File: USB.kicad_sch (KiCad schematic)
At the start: 29 parts, among them J11 USB3_A, J12 USB3_A, Q1 TCKE800NL, U14 USB5734_MR, Y3 25Mhz

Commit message: change cad data
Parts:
- removed R44: 10kΩ, Resistor_SMD:R_0603_1608Metric_Pad0.98x0.95mm_HandSolder, symbol Device:R
- removed U14: USB5734_MR, CM5IO:QFN50P900X900X100-65N, symbol USB5734:USB5734_MR
- added C137, C138, C139, C140, C142, C143, C144, C145, C87: 0.1uF, Capacitor_SMD:C_0402_1005Metric_Pad0.74x0.62mm_HandSolder, symbol Device:C
- added FB1: FerriteBead, Inductor_SMD:L_0603_1608Metric_Pad1.05x0.95mm_HandSolder, symbol Device:FerriteBead
- added R62: 320kΩ, Resistor_SMD:R_0603_1608Metric_Pad0.98x0.95mm_HandSolder, symbol Device:R
- added U15: USB5744_2G, CM5IO:VQFN56_2G_MCH, symbol USB5744:USB5744_2G
- C36: renamed from C22; footprint Capacitor_SMD:C_0603_1608Metric_Pad1.08x0.95mm_HandSolder -> Capacitor_SMD:C_0402_1005Metric_Pad0.74x0.62mm_HandSolder
- Y4: renamed from Y3; footprint Crystal:Crystal_SMD_SeikoEpson_FA238-4Pin_3.2x2.5mm -> Crystal:Crystal_SMD_SeikoEpson_FA128-4Pin_2.0x1.6mm
- renumbered C85 to C101, C87 to C105, C79 to C106, C96 to C118, C95 to C119, C97 to C120, C94 to C121, C23 to C37, C24 to C38, C25 to C39, C27 to C41, C28 to C42, C29 to C43, C51 to C73, C52 to C74, C62 to C82, C59 to C83, C60 to C84, C61 to C85, C75 to C99, R7 to R17, R42 to R53
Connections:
- net +3.3V: now also FB1.1; no longer C105.1, C120.1, C82.1, C84.1
- net 1.2V: now also U15.12 (VDD12__1), U15.15 (VDD12__2), U15.21 (VDD12__3), U15.28 (VDD12__4), U15.33 (VDD12__5), U15.43 (VDD12__6), U15.49 (VDD12__7), U15.5 (VDD12)
- net GND: now also C87.2, U15.52 (ATEST), U15.57 (VSS)
- net SS_RX_N: now also U15.51 (USB3UP_RXDM)
- net SS_RX_P: now also U15.50 (USB3UP_RXDP)
- net SS_TX_N: now also U15.48 (USB3UP_TXDM)
- net SS_TX_P: now also U15.47 (USB3UP_TXDP)
- net USB3-0-D_N: now also U15.2 (USB2DN_DM1/PRT_DIS_M1)
- net USB3-0-D_P: now also U15.1 (USB2DN_DP1/PRT_DIS_P1)
- net USB3-0-RX_N: now also U15.7 (USB3DN_RXDM1)
- net USB3-0-RX_P: now also U15.6 (USB3DN_RXDP1)
- net USB3-0-TX_N: now also C144.1, U15.4 (USB3DN_TXDM1); no longer J12.A8 (SSTX-)
- net USB3-0-TX_P: now also C145.1, U15.3 (USB3DN_TXDP1); no longer J12.A9 (SSTX+)
- net USB3-1-D_N: now also U15.9 (USB2DN_DM2/PRT_DIS_M2)
- net USB3-1-D_P: now also U15.8 (USB2DN_DP2/PRT_DIS_P2)
- net USB3-1-RX_N: now also U15.14 (USB3DN_RXDM2)
- net USB3-1-RX_P: now also U15.13 (USB3DN_RXDP2)
- net USB3-1-TX_N: now also C138.1, U15.11 (USB3DN_TXDM2); no longer J12.B9 (SSTX+)
- net USB3-1-TX_P: now also C137.1, U15.10 (USB3DN_TXDP2); no longer J12.B8 (SSTX-)
- net USB3-2-D_N: now also U15.18 (USB2DN_DM3/PRT_DIS_M3)
- net USB3-2-D_P: now also U15.17 (USB2DN_DP3/PRT_DIS_P3)
- net USB3-2-RX_N: now also U15.23 (USB3DN_RXDM3)
- net USB3-2-RX_P: now also U15.22 (USB3DN_RXDP3)
- net USB3-2-TX_N: now also C140.1, U15.20 (USB3DN_TXDM3); no longer J11.B9 (SSTX+)
- net USB3-2-TX_P: now also C139.1, U15.19 (USB3DN_TXDP3); no longer J11.B8 (SSTX-)
- net USB3-3-D_N: now also U15.25 (USB2DN_DM4/PRT_DIS_M4)
- net USB3-3-D_P: now also U15.24 (USB2DN_DP4/PRT_DIS_P4)
- net USB3-3-RX_N: now also U15.30 (USB3DN_RXDM4)
- net USB3-3-RX_P: now also U15.29 (USB3DN_RXDP4)
- net USB3-3-TX_N: now also C142.1, U15.27 (USB3DN_TXDM4); no longer J11.A8 (SSTX-)
- net USB3-3-TX_P: now also C143.1, U15.26 (USB3DN_TXDP4); no longer J11.A9 (SSTX+)
- net USB_DN: now also U15.46 (USB2UP_DM)
- net USB_DP: now also U15.45 (USB2UP_DP)
- net at C74.1, Y4.3: now also U15.53 (XTALO)
- net at C73.1, Y4.1: now also U15.54 (XTALI/CLK_IN)
- net at R53.2: now also U15.56 (RBIAS)
- new net: C87.1, R62.1, U15.42 (RESET_N)
- new net: C139.2, J11.B8 (SSTX-)
- new net: C140.2, J11.B9 (SSTX+)
- new net: C137.2, J12.B8 (SSTX-)
- new net: C143.2, J11.A9 (SSTX+)
- new net: C144.2, J12.A8 (SSTX-)
- new net: C142.2, J11.A8 (SSTX-)
- new net: C145.2, J12.A9 (SSTX+)
- new net: C138.2, J12.B9 (SSTX+)
- new net 3.3V: C105.1, C120.1, C82.1, C84.1, FB1.2, R62.2, U15.16 (VDD33), U15.31 (VDD33__1), U15.37 (VBUS_DET/GPIO16), U15.44 (VDD33__2), U15.55 (VDD33__3)
- no-connect marks 0 -> 4
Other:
- moved on the sheet: C105, C120, C73, C74, C82, C84, J11, J12, R53, Y4

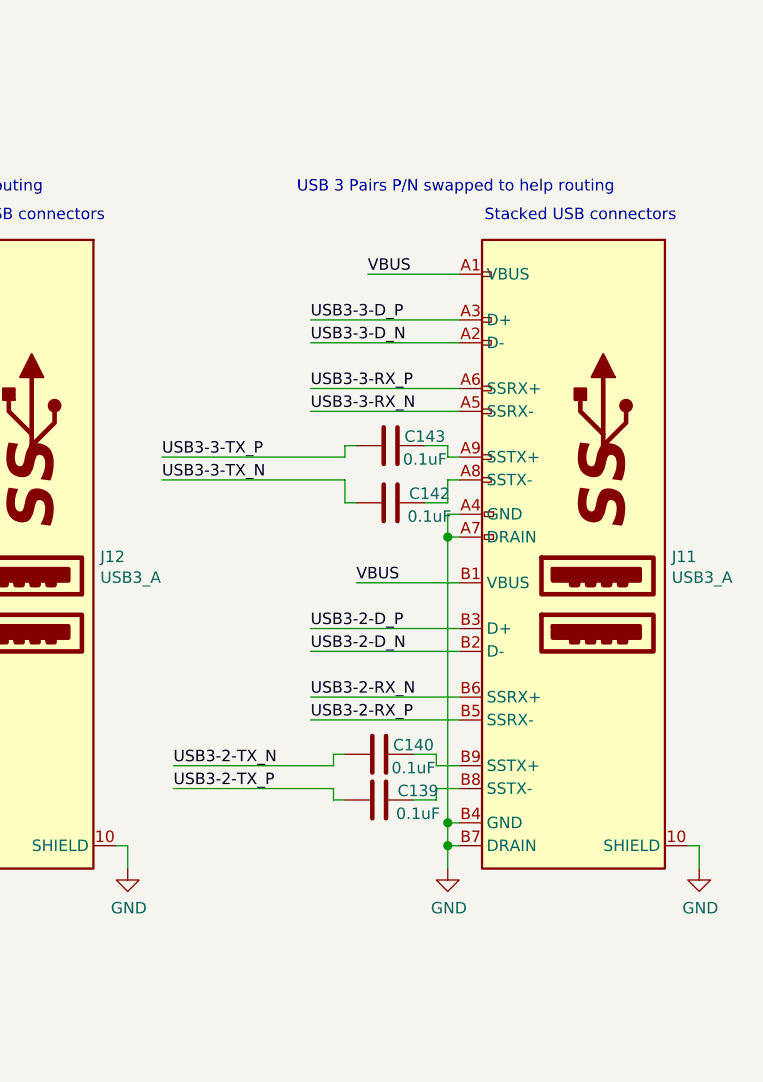
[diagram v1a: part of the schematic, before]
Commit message: change clearance
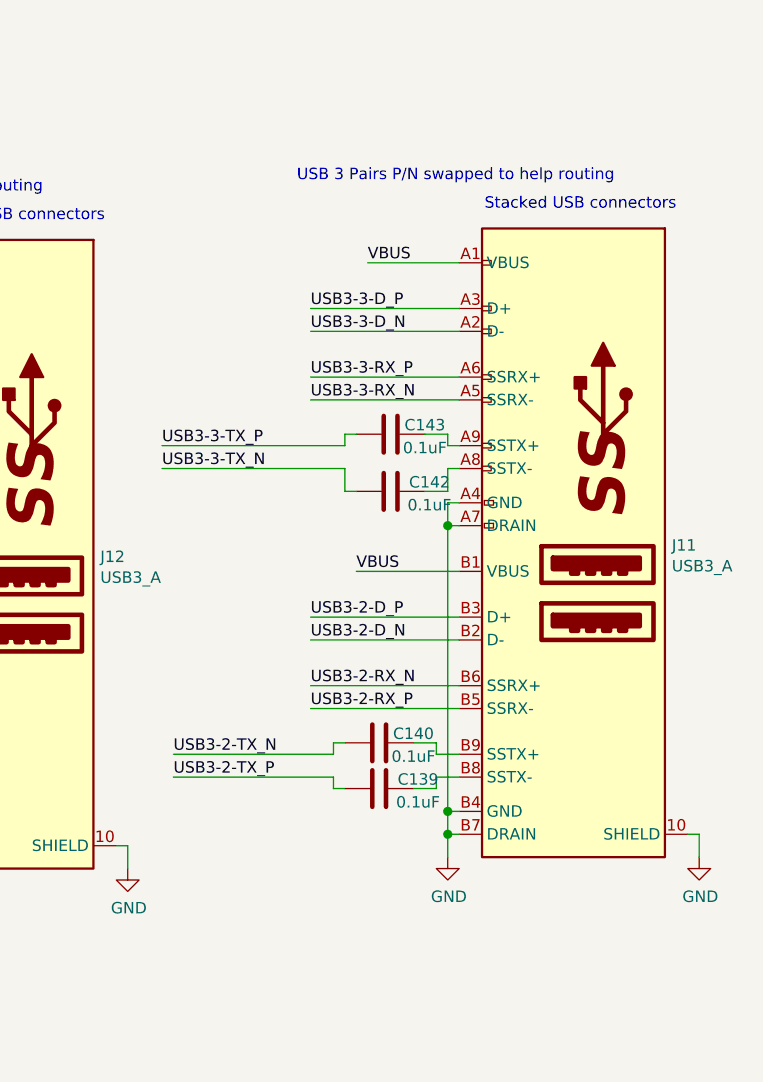
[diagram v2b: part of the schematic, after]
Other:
- moved on the sheet: C139, C140, C142, C143, J11

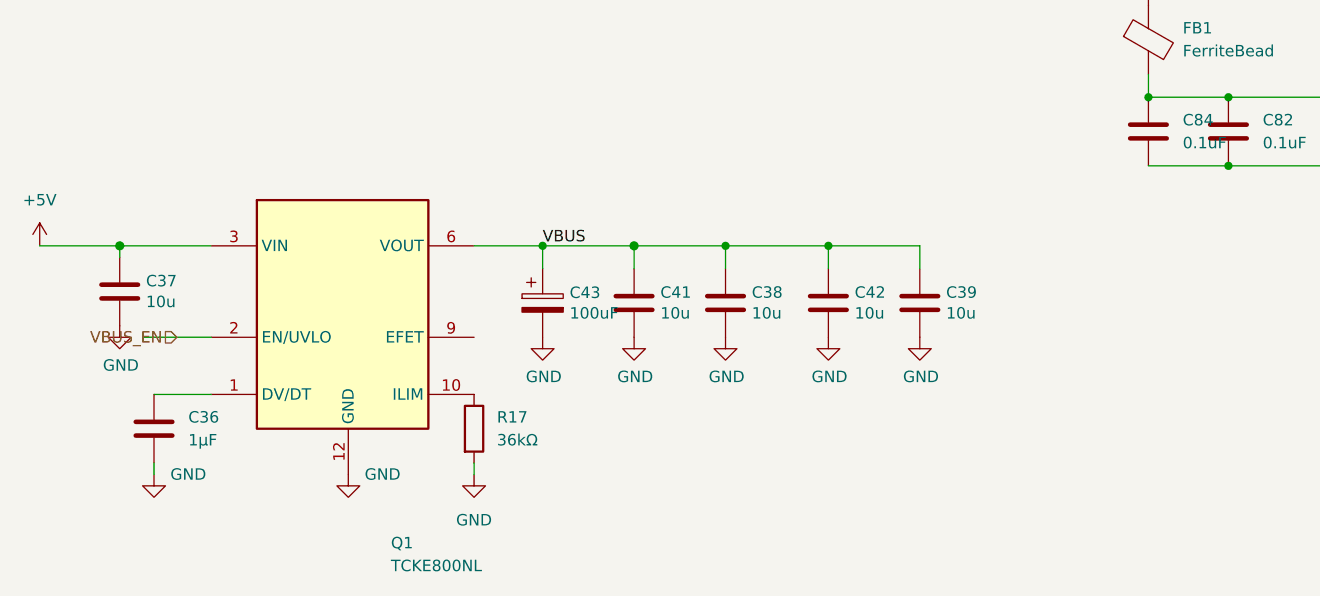
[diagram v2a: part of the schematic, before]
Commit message: change efuse
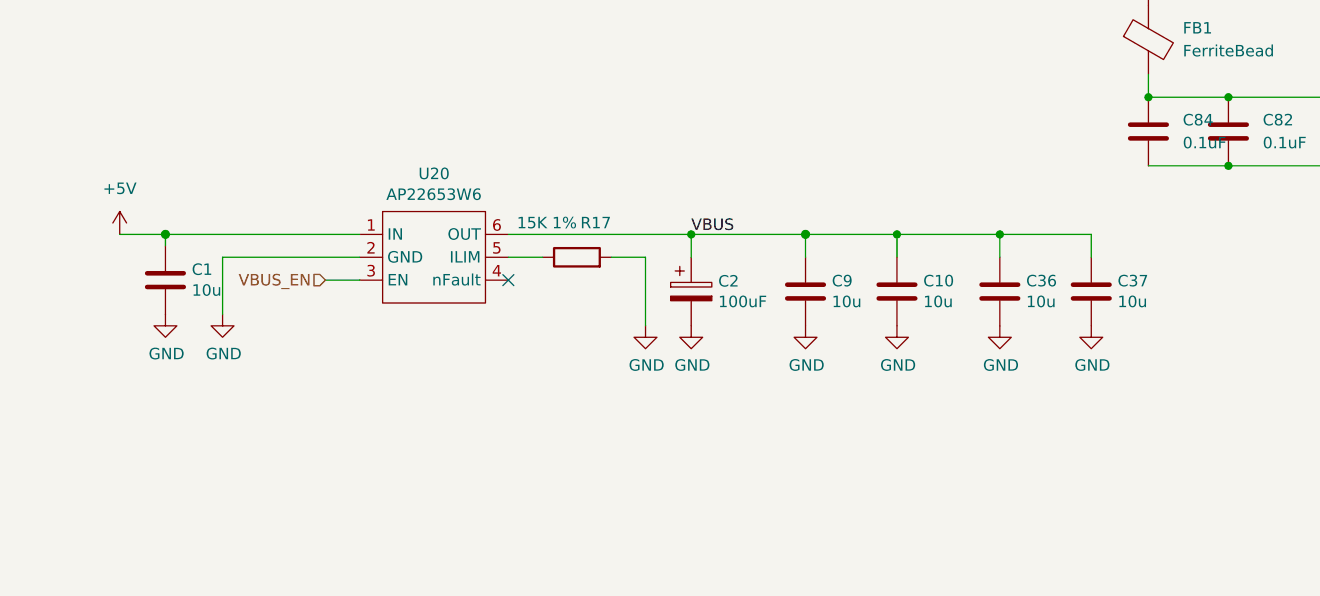
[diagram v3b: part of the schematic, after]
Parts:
- removed C38, C39, C41, C42: 10u, Capacitor_SMD:C_0805_2012Metric, symbol Device:C
- removed C43: 100uF, Capacitor_Tantalum_SMD:CP_EIA-7343-31_Kemet-D, symbol Device:C_Polarized
- removed Q1: TCKE800NL, CM5IO:TCKE800NL, symbol TCKE800NL:TCKE800NL
- added C1, C10, C9: 10u, Capacitor_SMD:C_0805_2012Metric, symbol Device:C
- added C2: 100uF, Capacitor_Tantalum_SMD:CP_EIA-7343-31_Kemet-D, symbol Device:C_Polarized
- added U20: AP22653W6, Package_TO_SOT_SMD:SOT-23-6, symbol CM5IO:AP2553W6
- C36: value 1μF -> 10u; footprint Capacitor_SMD:C_0402_1005Metric_Pad0.74x0.62mm_HandSolder -> Capacitor_SMD:C_0805_2012Metric; Field4 (none) -> Digikey; Field5 (none) -> 490-14381-1-ND; Field6 (none) -> GRM21BR71A106KA73L; Field7 (none) -> Murata; Field8 (none) -> 111893011; Part Description (none) -> 10uF 10% 10V Ceramic Capacitor X7R 0805 (2012 Metric)
- R17: value 36kΩ -> 15K 1%
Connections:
- net +5V: now also C1.1, U20.1 (IN); no longer C37.1
- net GND: now also C1.2, C10.2, C2.2, C9.2, U20.2 (GND)
- net VBUS: now also C36.1, C37.1, C10.1, C2.1, C9.1, U20.6 (OUT)
- net VBUS_EN: now also U20.3 (EN)
- net at R17.1: now also U20.5 (ILIM)
- no-connect marks 4 -> 5

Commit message: remove efuse
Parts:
- removed C10, C36, C37, C9: 10u, Capacitor_SMD:C_0805_2012Metric, symbol Device:C
- renumbered C118 to C107, C119 to C108, C120 to C109, C121 to C110, C139 to C127, C140 to C128, C137 to C129, C138 to C130, C142 to C132, C143 to C133, C144 to C134, C145 to C135, C1 to C32, C2 to C34, C73 to C63, C74 to C64, C82 to C72, C83 to C73, C85 to C74, C84 to C75, C87 to C77, C99 to C83, C101 to C90, C105 to C93, C106 to C95, R53 to R52, R62 to R59, U15 to U16, U20 to U8, Y4 to Y5
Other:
- moved on the sheet: C34

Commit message: add sata capacitor
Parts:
- renumbered C90 to C100, C93 to C104, C95 to C105, C108 to C117, C107 to C118, C109 to C119, C110 to C120, C128 to C137, C127 to C138, C130 to C139, C129 to C140, C133 to C142, C132 to C143, C135 to C144, C134 to C145, C32 to C40, C34 to C42, C64 to C73, C63 to C74, C73 to C82, C72 to C83, C74 to C84, C75 to C85, C77 to C87, C83 to C93, J12 to J11, J11 to J12, R52 to R53, R59 to R61

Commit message: change design
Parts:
- renumbered C100 to C102, C93 to C94
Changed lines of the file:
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@@
 		(dnp no)
 		(fields_autoplaced yes)
-		(property "Reference" "C93"
+		(property "Reference" "C94"
 			(at 242.57 154.9399 0)
 			(effects
@@
 			(project "mainboard4"
 				(path "/dd07ab80-a59c-44f4-ac7d-849e21e1384e/8b7f7566-5318-467c-baab-209769ce6529"
-					(reference "C93")
+					(reference "C94")
 					(unit 1)
 				)
@@
 		(dnp no)
 		(fields_autoplaced yes)
-		(property "Reference" "C100"
+		(property "Reference" "C102"
 			(at 217.17 154.9399 0)
 			(effects
@@
 			(project "mainboard4"
 				(path "/dd07ab80-a59c-44f4-ac7d-849e21e1384e/8b7f7566-5318-467c-baab-209769ce6529"
-					(reference "C100")
-					(unit 1)
-				)
+					(reference "C102")
+					(unit 1)
+				)

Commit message: add logp
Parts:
- added R60: 10Ω, Resistor_SMD:R_0603_1608Metric, symbol Device:R
- R56: renamed from R61; footprint Resistor_SMD:R_0603_1608Metric_Pad0.98x0.95mm_HandSolder -> Resistor_SMD:R_0603_1608Metric
- renumbered C85 to C84, C87 to C85, C84 to C86, R17 to R14, R53 to R50
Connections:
- net GND: now also R60.1
- net at U16.40 (SPI_DI/CFG_BC_EN/GPIO9): now also R60.2
